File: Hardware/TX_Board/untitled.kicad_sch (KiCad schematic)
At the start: 42 parts, among them IC7 MAPS-010164-TR0500, IC8 QPA9122TR7, J13 MM8030-2610RJ3, J14 MM8030-2610RJ3, J15 Conn_Coaxial

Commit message: Updated Layout
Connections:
- net at IC8.2 (RFIN): now also C28.2; no longer J14.2 (OUT)
- net at C28.1: now also J14.2 (OUT); no longer AT1.9 (RFOUT)
- net at J14.1 (IN): now also AT1.9 (RFOUT); no longer C28.2
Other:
- moved on the sheet: C28
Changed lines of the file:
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@@
 	(wire
 		(pts
-			(xy 229.87 151.13) (xy 266.7 151.13)
-		)
-		(stroke
-			(width 0)
-			(type default)
-		)
-	)
-	(wire
-		(pts
 			(xy 335.28 107.95) (xy 335.28 92.71)
 		)
@@
 	(wire
 		(pts
-			(xy 294.64 151.13) (xy 307.34 151.13)
-		)
-		(stroke
-			(width 0)
-			(type default)
-		)
-	)
-	(wire
-		(pts
 			(xy 222.25 133.35) (xy 222.25 135.89)
 		)
@@
 	(wire
 		(pts
-			(xy 208.28 151.13) (xy 222.25 151.13)
+			(xy 167.64 143.51) (xy 177.8 143.51)
 		)
 		(stroke
@@
 	(wire
 		(pts
-			(xy 167.64 143.51) (xy 177.8 143.51)
+			(xy 49.53 151.13) (xy 58.42 151.13)
 		)
 		(stroke
@@
 	(wire
 		(pts
-			(xy 49.53 151.13) (xy 58.42 151.13)
+			(xy 208.28 151.13) (xy 266.7 151.13)
 		)
 		(stroke
@@
 	(wire
 		(pts
+			(xy 302.26 151.13) (xy 307.34 151.13)
+		)
+		(stroke
+			(width 0)
+			(type default)
+		)
+	)
+	(wire
+		(pts
 			(xy 187.96 168.91) (xy 187.96 172.72)
 		)
@@
 	(symbol
 		(lib_id "tx_board_symbol_library:C")
-		(at 226.06 151.13 90)
+		(at 298.45 151.13 90)
 		(unit 1)
 		(exclude_from_sim no)
@@
 		(dnp no)
 		(property "Reference" "C28"
-			(at 226.06 157.734 90)
+			(at 298.45 157.734 90)
 			(effects
 				(font
@@
 		)
 		(property "Value" "18 pF"
-			(at 226.06 154.94 90)
+			(at 298.45 154.94 90)
 			(effects
 				(font
@@
 		)
 		(property "Footprint" "Capacitor_SMD:C_0402_1005Metric"
-			(at 229.87 150.1648 0)
+			(at 302.26 150.1648 0)
 			(effects
 				(font
@@
 		)
 		(property "Datasheet" "~"
-			(at 226.06 151.13 0)
+			(at 298.45 151.13 0)
 			(effects
 				(font
@@
 		)
 		(property "Description" "Unpolarized capacitor"
-			(at 226.06 151.13 0)
+			(at 298.45 151.13 0)
 			(effects
 				(font

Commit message: More Layout
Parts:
- added C105: 1 uF, Capacitor_SMD:C_0402_1005Metric, symbol tx_board_symbol_library:C
- added C106: 100 pF, Capacitor_SMD:C_0402_1005Metric, symbol tx_board_symbol_library:C
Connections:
- net GND: now also C105.1, C106.1
- net at IC8.16 (VPD), R26.2: now also C105.2, C106.2

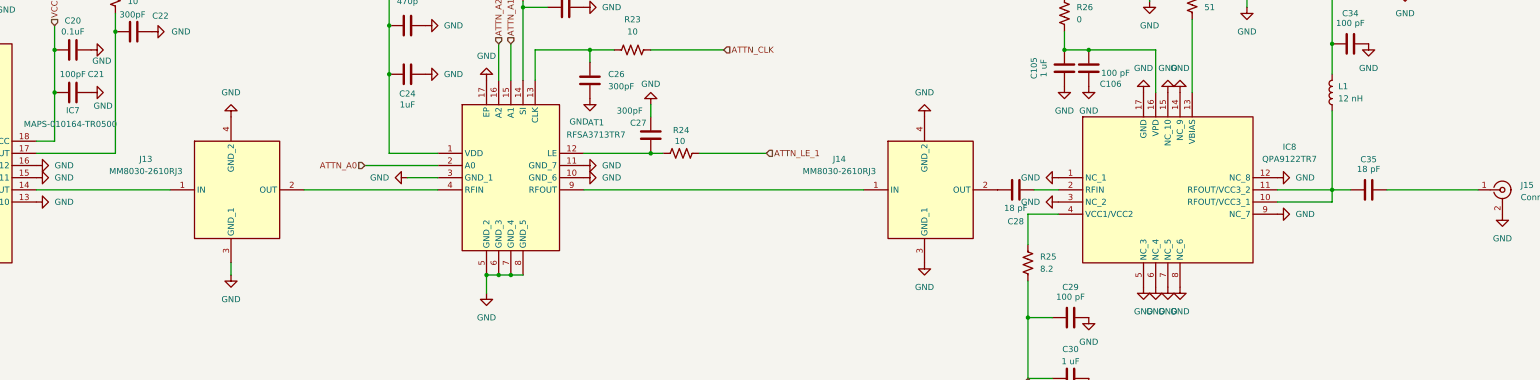
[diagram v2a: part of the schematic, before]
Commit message: Waveguide + ground planes and P.S. daughter board modification
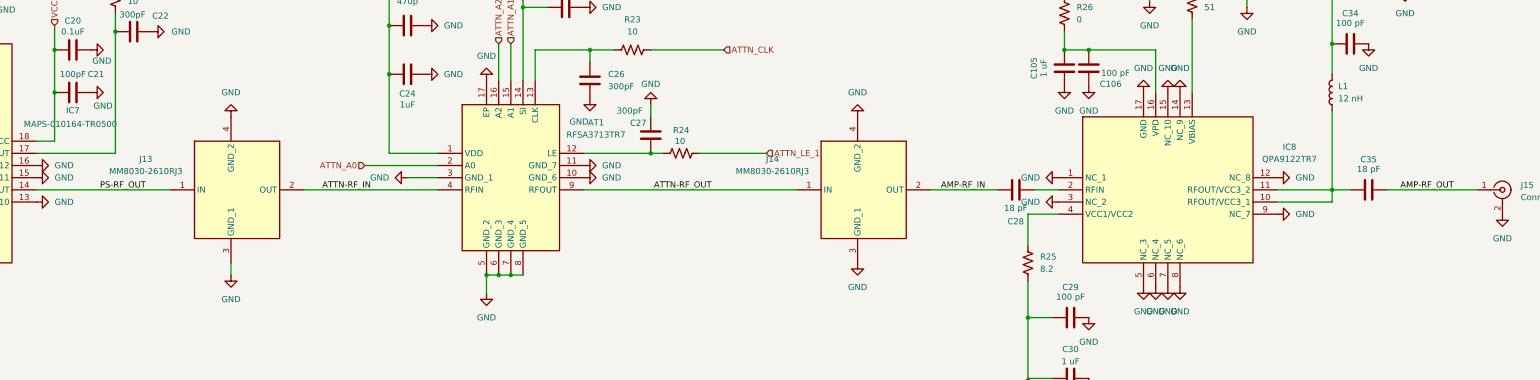
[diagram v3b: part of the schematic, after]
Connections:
- net PS-RF_OUT: now reaches IC7.14 (RF_OUT), J13.1 (IN)
- net AMP-RF_IN: now reaches C28.1, J14.2 (OUT)
- net ATTN-RF_IN: now reaches AT1.4 (RFIN), J13.2 (OUT)
- net ATTN-RF_OUT: now reaches AT1.9 (RFOUT), J14.1 (IN)
- net AMP-RF_OUT: now reaches C35.2, J15.1 (In)
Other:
- moved on the sheet: J14

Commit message: Ease of construction, added new layers, prelimininary routing.
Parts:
- C105, C106, C13, C14, C15, C16, C17, C18, C19, C20, C21, C22, C23, C24, C25, C26, C27, C29, C30, C31, C32, C33, C34: footprint Capacitor_SMD:C_0402_1005Metric -> Capacitor_SMD:C_0603_1608Metric
- L1: footprint Inductor_SMD:L_0402_1005Metric -> Inductor_SMD:L_0603_1608Metric
- R18, R19, R20, R21, R22, R23, R24, R25, R26, R27, R28, R29: footprint Resistor_SMD:R_0402_1005Metric -> Resistor_SMD:R_0603_1608Metric
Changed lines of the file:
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@@
 			)
 		)
-		(property "Footprint" "Resistor_SMD:R_0402_1005Metric"
+		(property "Footprint" "Resistor_SMD:R_0603_1608Metric"
 			(at 299.974 166.116 90)
 			(effects
@@
 			)
 		)
-		(property "Footprint" "Capacitor_SMD:C_0402_1005Metric"
+		(property "Footprint" "Capacitor_SMD:C_0603_1608Metric"
 			(at 175.26 115.8748 0)
 			(effects
@@
 			)
 		)
-		(property "Footprint" "Capacitor_SMD:C_0402_1005Metric"
+		(property "Footprint" "Capacitor_SMD:C_0603_1608Metric"
 			(at 118.11 117.1448 0)
 			(effects
@@
 			)
 		)
-		(property "Footprint" "Resistor_SMD:R_0402_1005Metric"
+		(property "Footprint" "Resistor_SMD:R_0603_1608Metric"
 			(at 72.136 101.854 90)
 			(effects
@@
 			)
 		)
-		(property "Footprint" "Resistor_SMD:R_0402_1005Metric"
+		(property "Footprint" "Resistor_SMD:R_0603_1608Metric"
 			(at 363.474 100.076 90)
 			(effects
@@
 			)
 		)
-		(property "Footprint" "Resistor_SMD:R_0402_1005Metric"
+		(property "Footprint" "Resistor_SMD:R_0603_1608Metric"
 			(at 309.626 114.554 90)
 			(effects
@@
 			)
 		)
-		(property "Footprint" "Resistor_SMD:R_0402_1005Metric"
+		(property "Footprint" "Resistor_SMD:R_0603_1608Metric"
 			(at 196.596 108.204 90)
 			(effects
@@
 			)
 		)
-		(property "Footprint" "Capacitor_SMD:C_0402_1005Metric"
+		(property "Footprint" "Capacitor_SMD:C_0603_1608Metric"
 			(at 41.6052 140.97 0)
 			(effects
@@
 			)
 		)
-		(property "Footprint" "Resistor_SMD:R_0402_1005Metric"
+		(property "Footprint" "Resistor_SMD:R_0603_1608Metric"
 			(at 218.694 120.904 90)
 			(effects
@@
 			)
 		)
-		(property "Footprint" "Resistor_SMD:R_0402_1005Metric"
+		(property "Footprint" "Resistor_SMD:R_0603_1608Metric"
 			(at 87.884 100.584 90)
 			(effects
@@
 			)
 		)
-		(property "Footprint" "Resistor_SMD:R_0402_1005Metric"
+		(property "Footprint" "Resistor_SMD:R_0603_1608Metric"
 			(at 111.506 110.744 90)
 			(effects
@@
 			)
 		)
-		(property "Footprint" "Capacitor_SMD:C_0402_1005Metric"
+		(property "Footprint" "Capacitor_SMD:C_0603_1608Metric"
 			(at 105.41 120.9548 0)
 			(effects
@@
 			)
 		)
-		(property "Footprint" "Resistor_SMD:R_0402_1005Metric"
+		(property "Footprint" "Resistor_SMD:R_0603_1608Metric"
 			(at 341.884 91.694 90)
 			(effects
@@
 			)
 		)
-		(property "Footprint" "Resistor_SMD:R_0402_1005Metric"
+		(property "Footprint" "Resistor_SMD:R_0603_1608Metric"
 			(at 83.566 88.646 90)
 			(effects
@@
 			)
 		)
-		(property "Footprint" "Capacitor_SMD:C_0402_1005Metric"
+		(property "Footprint" "Capacitor_SMD:C_0603_1608Metric"
 			(at 41.6052 151.13 0)
 			(effects
@@
 			)
 		)
-		(property "Footprint" "Inductor_SMD:L_0402_1005Metric"
+		(property "Footprint" "Inductor_SMD:L_0603_1608Metric"
 			(at 364.49 130.81 0)
 			(effects
@@
 			)
 		)
-		(property "Footprint" "Capacitor_SMD:C_0402_1005Metric"
+		(property "Footprint" "Capacitor_SMD:C_0603_1608Metric"
 			(at 73.66 94.9452 0)
 			(effects
@@
 			)
 		)
-		(property "Footprint" "Resistor_SMD:R_0402_1005Metric"
+		(property "Footprint" "Resistor_SMD:R_0603_1608Metric"
 			(at 336.296 112.014 90)
 			(effects
@@
 			)
 		)
-		(property "Footprint" "Capacitor_SMD:C_0402_1005Metric"
+		(property "Footprint" "Capacitor_SMD:C_0603_1608Metric"
 			(at 372.11 108.2548 0)
 			(effects
@@
 			)
 		)
-		(property "Footprint" "Capacitor_SMD:C_0402_1005Metric"
+		(property "Footprint" "Capacitor_SMD:C_0603_1608Metric"
 			(at 334.01 106.9848 0)
 			(effects
@@
 			)
 		)
-		(property "Footprint" "Capacitor_SMD:C_0402_1005Metric"
+		(property "Footprint" "Capacitor_SMD:C_0603_1608Metric"
 			(at 313.69 176.8348 0)
 			(effects
@@
 			)
 		)
-		(property "Footprint" "Capacitor_SMD:C_0402_1005Metric"
+		(property "Footprint" "Capacitor_SMD:C_0603_1608Metric"
 			(at 76.2 107.6452 0)
 			(effects
@@
 			)
 		)
-		(property "Footprint" "Capacitor_SMD:C_0402_1005Metric"
+		(property "Footprint" "Capacitor_SMD:C_0603_1608Metric"
 			(at 50.4952 140.97 0)
 			(effects
@@
 			)
 		)
-		(property "Footprint" "Capacitor_SMD:C_0402_1005Metric"
+		(property "Footprint" "Capacitor_SMD:C_0603_1608Metric"
 			(at 372.11 119.6848 0)
 			(effects
@@
 			)
 		)
-		(property "Footprint" "Capacitor_SMD:C_0402_1005Metric"
+		(property "Footprint" "Capacitor_SMD:C_0603_1608Metric"
 			(at 97.79 131.7752 0)
 			(effects
@@
 			)
 		)
-		(property "Footprint" "Capacitor_SMD:C_0402_1005Metric"
+		(property "Footprint" "Capacitor_SMD:C_0603_1608Metric"
 			(at 175.26 126.0348 0)
 			(effects
@@
 			)
 		)
-		(property "Footprint" "Capacitor_SMD:C_0402_1005Metric"
+		(property "Footprint" "Capacitor_SMD:C_0603_1608Metric"
 			(at 312.7248 121.92 0)
 			(effects
@@
 			)
 		)
-		(property "Footprint" "Capacitor_SMD:C_0402_1005Metric"
+		(property "Footprint" "Capacitor_SMD:C_0603_1608Metric"
 			(at 346.71 106.9848 0)
 			(effects
@@
 			)
 		)
-		(property "Footprint" "Capacitor_SMD:C_0402_1005Metric"
+		(property "Footprint" "Capacitor_SMD:C_0603_1608Metric"
 			(at 313.69 189.5348 0)
 			(effects
@@
 			)
 		)
-		(property "Footprint" "Resistor_SMD:R_0402_1005Metric"
+		(property "Footprint" "Resistor_SMD:R_0603_1608Metric"
 			(at 228.854 142.494 90)
 			(effects
@@
 			)
 		)
-		(property "Footprint" "Capacitor_SMD:C_0402_1005Metric"
+		(property "Footprint" "Capacitor_SMD:C_0603_1608Metric"
 			(at 59.69 108.9152 0)
 			(effects
@@
 			)
 		)
-		(property "Footprint" "Capacitor_SMD:C_0402_1005Metric"
+		(property "Footprint" "Capacitor_SMD:C_0603_1608Metric"
 			(at 307.6448 121.92 0)
 			(effects
@@
 			)
 		)
-		(property "Footprint" "Capacitor_SMD:C_0402_1005Metric"
+		(property "Footprint" "Capacitor_SMD:C_0603_1608Metric"
 			(at 223.2152 143.51 0)
 			(effects
@@
 			)
 		)
-		(property "Footprint" "Capacitor_SMD:C_0402_1005Metric"
+		(property "Footprint" "Capacitor_SMD:C_0603_1608Metric"
 			(at 33.9852 151.13 0)
 			(effects
@@
 			)
 		)
-		(property "Footprint" "Capacitor_SMD:C_0402_1005Metric"
+		(property "Footprint" "Capacitor_SMD:C_0603_1608Metric"
 			(at 210.5152 132.08 0)
 			(effects
@@
 			)
 		)
-		(property "Footprint" "Capacitor_SMD:C_0402_1005Metric"
+		(property "Footprint" "Capacitor_SMD:C_0603_1608Metric"
 			(at 208.28 112.0648 0)
 			(effects

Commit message: DRC and more layout
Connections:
- net ATTN_A0 is gone; now on net GND: AT1.2 (A0)
- net ATTN_A1 is gone; now on net GND: AT1.15 (A1)
- net ATTN_A2 is gone; now on net GND: AT1.16 (A2)

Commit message: Testing Data
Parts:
- removed J15: Conn_Coaxial, Connector_Coaxial:SMA_Amphenol_132289_EdgeMount, symbol tx_board_symbol_library:Conn_Coaxial
- removed R29: 0, Resistor_SMD:R_0603_1608Metric, symbol tx_board_symbol_library:R_US
- added HY1: BDCA1-10-40+, BDCA1-10-40+:BDCA11040, symbol BDCA1-10-40+:BDCA1-10-40+
- added J24: Conn_Coaxial, Connector_Coaxial:SMA_Samtec_SMA-J-P-H-ST-EM1_EdgeMount, symbol Connector:Conn_Coaxial
- added J6: Conn_Coaxial, Connector_Coaxial:SMA_Amphenol_901-144_Vertical, symbol Connector:Conn_Coaxial
- added L13, L17, L21, L25, L29, L5, L9: L_Ferrite, Inductor_SMD:L_0201_0603Metric_Pad0.64x0.40mm_HandSolder, symbol Device:L_Ferrite
- added R66: 50, Resistor_SMD:R_0402_1005Metric, symbol tx_board_symbol_library:R_US
- C17, C18, C19, C22, C25, C26, C27: value 300pF -> 1.3 pF
- R18, R19, R20, R21, R22, R23, R24: value 10 -> 50
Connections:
- net AMP-RF_OUT: now also HY1.1 (INPUT)
- net GND: now also HY1.2 (GROUND_1), HY1.3 (GROUND_2), HY1.4 (GROUND_3), HY1.7 (GROUND_4), HY1.8 (GROUND_5), HY1.9 (GROUND_6), J24.2 (Ext), J6.2 (Ext), R66.2
- net VCC: now also L17.1, L25.1, L29.2, L5.1, L9.1; no longer AT1.1 (VDD), C15.1, C21.2, C24.1, C29.1, IC7.18 (VCC), IC7.2 (P/S), R25.1
- net VEE: now also L13.1; no longer C16.2, IC7.1 (VEE)
- net at C33.1, C34.1, L1.2: now also L29.1
- net at C105.2, R26.2: now also L21.1; no longer C106.2, IC8.16 (VPD)
- new net: C16.2, IC7.1 (VEE), L13.2
- new net: C21.2, IC7.18 (VCC), L9.2
- new net: C15.1, IC7.2 (P/S), L17.2
- new net: C29.1, L25.2, R25.1
- new net: AT1.1 (VDD), C24.1, L5.2
- new net: HY1.5 (COUPLED_(REVERSE)), R66.1
- new net: C106.2, IC8.16 (VPD), L21.2
- new net CPL_FWD: HY1.10 (COUPLED_(FORWARD)), J6.1 (In)
- new net OUTPUT: HY1.6 (OUTPUT), J24.1 (In)
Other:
- moved on the sheet: C106, C20
